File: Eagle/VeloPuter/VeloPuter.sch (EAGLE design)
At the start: 56 parts, among them IC2 B7546, IC3 B7546, Q1 4P04L04, Q10 4P04L04, Q11 BS170, Q12 4P04L04, Q13 BS170, Q14 4P04L04, Q2 BS170, Q3 BS170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

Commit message: Minor layout change
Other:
- moved on the sheet: Q3, Q4, R1
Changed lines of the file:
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@@
 <instance part="AUX_OUT" gate=".5" x="208.28" y="73.66" rot="R180"/>
 <instance part="AUX_OUT" gate=".6" x="208.28" y="66.04" rot="R180"/>
-<instance part="Q3" gate="1" x="317.5" y="162.56"/>
-<instance part="Q4" gate="G$1" x="330.2" y="167.64" rot="MR180"/>
-<instance part="R1" gate="G$1" x="322.58" y="170.18" rot="R90">
-<attribute name="OC_NEWARK" x="322.58" y="170.18" size="1.778" layer="96" display="off"/>
-<attribute name="MF" x="322.58" y="170.18" size="1.778" layer="96" display="off"/>
-<attribute name="MPN" x="322.58" y="170.18" size="1.778" layer="96" display="off"/>
+<instance part="Q3" gate="1" x="317.5" y="165.1"/>
+<instance part="Q4" gate="G$1" x="330.2" y="172.72" rot="MR180"/>
+<instance part="R1" gate="G$1" x="322.58" y="175.26" rot="R90">
+<attribute name="OC_NEWARK" x="322.58" y="175.26" size="1.778" layer="96" display="off"/>
+<attribute name="MF" x="322.58" y="175.26" size="1.778" layer="96" display="off"/>
+<attribute name="MPN" x="322.58" y="175.26" size="1.778" layer="96" display="off"/>
 </instance>
 <instance part="JP1" gate="A" x="327.66" y="149.86" rot="R270"/>
@@
 <segment>
 <pinref part="Q3" gate="1" pin="S"/>
-<wire x1="320.04" y1="157.48" x2="325.12" y2="160.02" width="0.1524" layer="91"/>
+<wire x1="320.04" y1="160.02" x2="325.12" y2="160.02" width="0.1524" layer="91"/>
 <pinref part="GND16" gate="1" pin="GND"/>
 </segment>
@@
 <pinref part="Q4" gate="G$1" pin="S"/>
 <wire x1="332.74" y1="154.94" x2="335.28" y2="154.94" width="0.1524" layer="91"/>
-<wire x1="332.74" y1="162.56" x2="332.74" y2="154.94" width="0.1524" layer="91"/>
+<wire x1="332.74" y1="167.64" x2="332.74" y2="154.94" width="0.1524" layer="91"/>
 <junction x="332.74" y="154.94"/>
 </segment>
@@
 <net name="PWM_FRONT" class="0">
 <segment>
-<wire x1="307.34" y1="165.1" x2="312.42" y2="162.56" width="0.1524" layer="91"/>
+<wire x1="307.34" y1="165.1" x2="312.42" y2="165.1" width="0.1524" layer="91"/>
 <pinref part="Q3" gate="1" pin="G"/>
 <label x="307.34" y="165.1" size="1.778" layer="95" rot="R180" xref="yes"/>
@@
 <label x="149.86" y="12.7" size="1.778" layer="95" xref="yes"/>
 <wire x1="142.24" y1="12.7" x2="149.86" y2="12.7" width="0.1524" layer="91"/>
+<junction x="142.24" y="12.7"/>
 </segment>
 </net>
@@
 <pinref part="R1" gate="G$1" pin="2"/>
 <pinref part="Q4" gate="G$1" pin="D"/>
-<wire x1="332.74" y1="175.26" x2="332.74" y2="172.72" width="0.1524" layer="91"/>
-<wire x1="332.74" y1="175.26" x2="322.58" y2="175.26" width="0.1524" layer="91"/>
+<wire x1="332.74" y1="180.34" x2="332.74" y2="177.8" width="0.1524" layer="91"/>
+<wire x1="332.74" y1="180.34" x2="322.58" y2="180.34" width="0.1524" layer="91"/>
 <label x="317.5" y="175.26" size="1.778" layer="95" rot="R180"/>
-<wire x1="317.5" y1="175.26" x2="322.58" y2="175.26" width="0.1524" layer="91"/>
-<junction x="322.58" y="175.26"/>
+<wire x1="317.5" y1="180.34" x2="322.58" y2="180.34" width="0.1524" layer="91"/>
+<junction x="322.58" y="180.34"/>
 </segment>
 <segment>
@@
 <pinref part="Q4" gate="G$1" pin="G"/>
 <pinref part="R1" gate="G$1" pin="1"/>
-<junction x="320.04" y="167.64"/>
-<wire x1="320.04" y1="167.64" x2="325.12" y2="165.1" width="0.1524" layer="91"/>
-<wire x1="322.58" y1="165.1" x2="320.04" y2="167.64" width="0.1524" layer="91"/>
-</segment>
-</net>
+<junction x="320.04" y="170.18"/>
+<wire x1="320.04" y1="170.18" x2="325.12" y2="170.18" width="0.1524" layer="91"/>
+<wire x1="322.58" y1="170.18" x2="320.04" y2="170.18" width="0.1524" layer="91"/>
+</segment>
+</net>

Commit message: Board updates
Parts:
- R6: value 1 ohm -> 1 Ω
- renumbered JP6 to JP
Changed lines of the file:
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@@
 <attribute name="OC_NEWARK" value="unknown"/>
 </part>
-<part name="R6" library="resistor" deviceset="R-EU_" device="0207/10" value="1 ohm">
+<part name="R6" library="resistor" deviceset="R-EU_" device="0207/10" value="1 Ω">
 <attribute name="MF" value=""/>
 <attribute name="MPN" value=""/>
@@
 <attribute name="OC_NEWARK" value="unknown"/>
 </part>
-<part name="JP6" library="jumper" deviceset="JP1E" device="" value=" "/>
+<part name="JP" library="jumper" deviceset="JP1E" device="" value=" "/>
 <part name="GND26" library="supply1" deviceset="GND" device=""/>
 <part name="GND27" library="supply1" deviceset="GND" device=""/>
@@
 <attribute name="MPN" x="322.58" y="-7.62" size="1.778" layer="96" display="off"/>
 </instance>
-<instance part="JP6" gate="A" x="327.66" y="-27.94" rot="R270"/>
+<instance part="JP" gate="A" x="327.66" y="-27.94" rot="R270"/>
 <instance part="GND26" gate="1" x="320.04" y="-30.48"/>
 <instance part="GND27" gate="1" x="325.12" y="-20.32"/>
@@
 <segment>
 <pinref part="GND26" gate="1" pin="GND"/>
-<pinref part="JP6" gate="A" pin="1"/>
+<pinref part="JP" gate="A" pin="1"/>
 <wire x1="320.04" y1="-27.94" x2="325.12" y2="-27.94" width="0.1524" layer="91"/>
 </segment>
@@
 <pinref part="U$1" gate="G$1" pin="DCOUT-"/>
 <pinref part="AUX_OUT" gate=".4" pin="SK"/>
-<pinref part="JP6" gate="A" pin="2"/>
+<pinref part="JP" gate="A" pin="2"/>
 <wire x1="325.12" y1="-30.48" x2="325.12" y2="-33.02" width="0.1524" layer="91"/>
 <wire x1="309.88" y1="-33.02" x2="325.12" y2="-33.02" width="0.1524" layer="91"/>

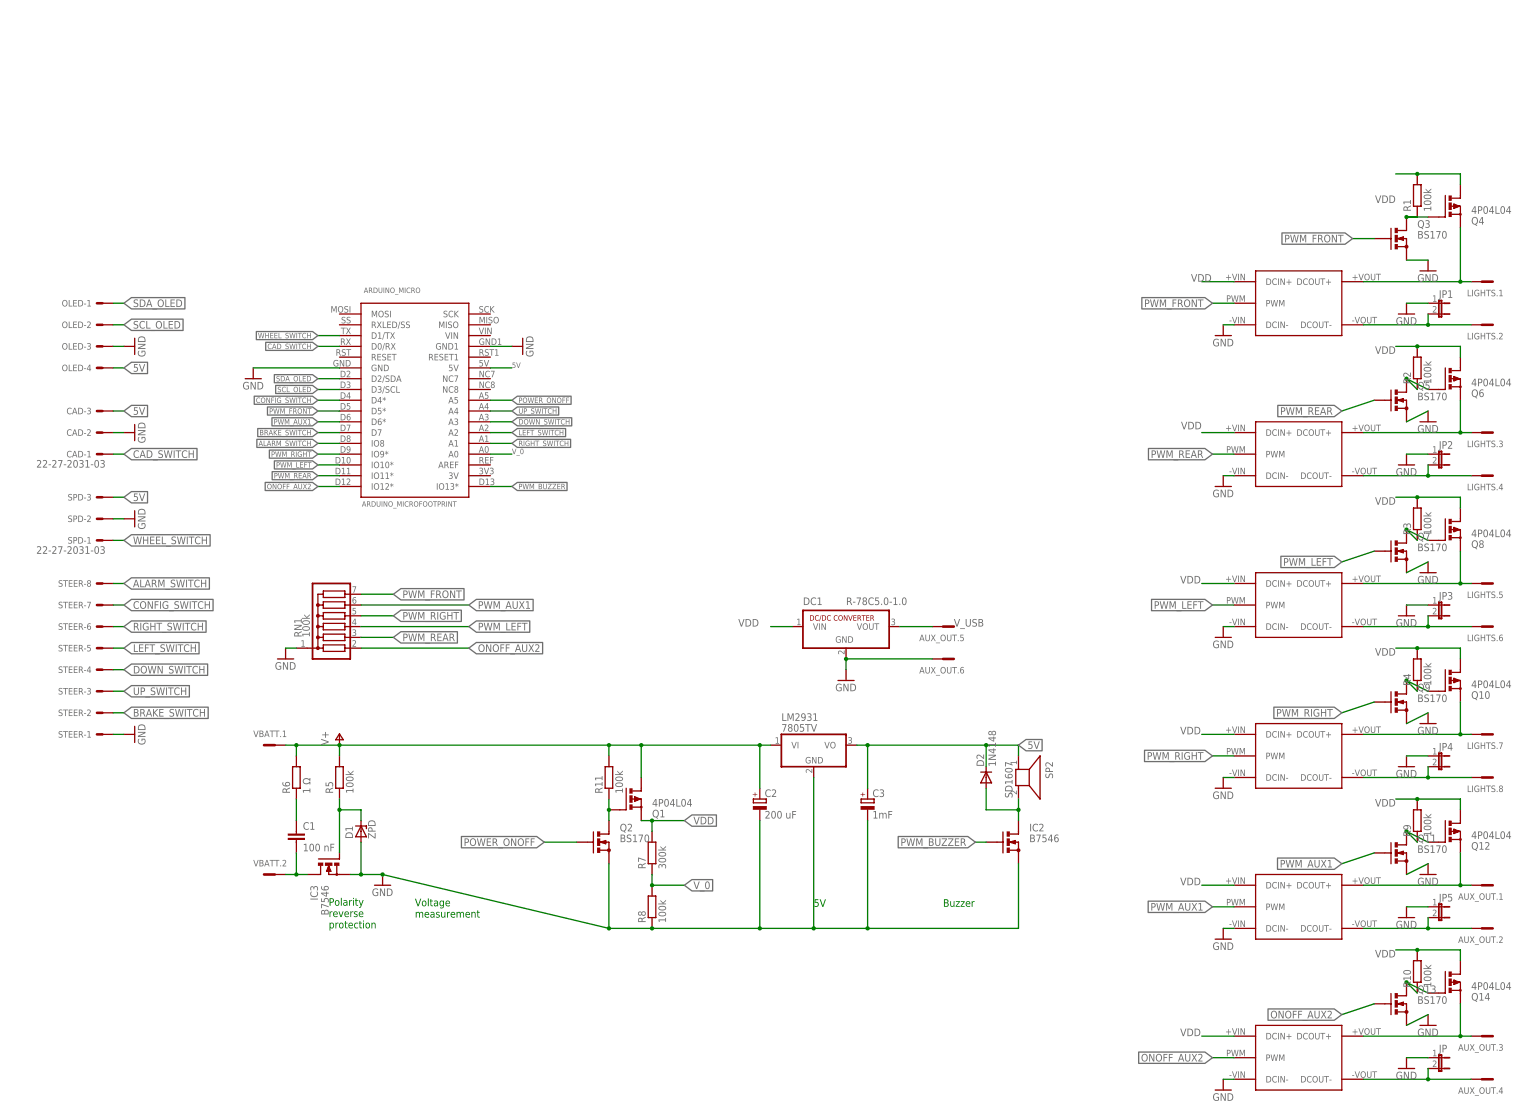
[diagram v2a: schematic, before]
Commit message: Board version 1.4 Suitable for the QV with new headlights
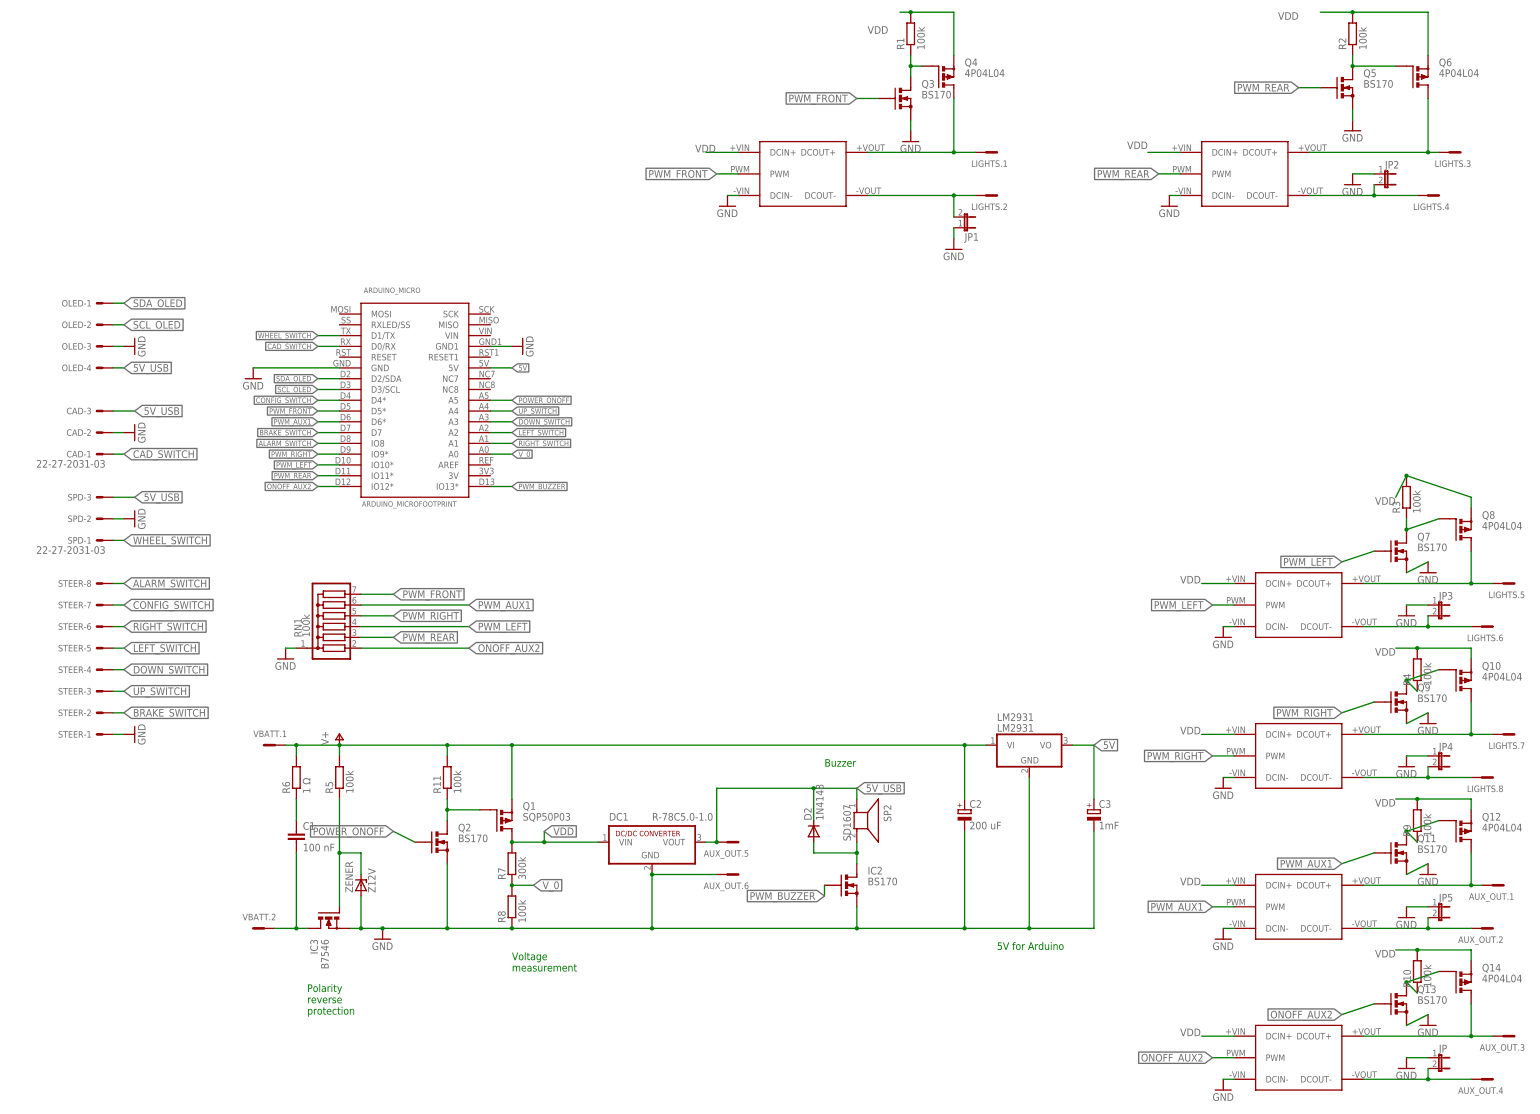
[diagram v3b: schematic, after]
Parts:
- removed D1: ZPD, diode:ZPD
- added ZENER: Z12V, diode:ZENER-DIODEDO34-7
- IC2: value B7546 -> BS170
- LM2931: value 7805TV -> LM2931
- Q1: value 4P04L04 -> SQP50P03
- R1, R10, R11, R2, R3, R4, R5, R6, R7, R8, R9: device resistor:R-EU_0207/10 -> resistor:R-EU_0207/7
- VBATT: value (none) -> VBatt
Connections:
- removed net V_USB: AUX_OUT.5.SK, DC1.VOUT
- new net 5V_USB: AUX_OUT.5.SK, CAD-3.S, D2.C, DC1.VOUT, OLED-4.S, SP2.1, SPD-3.S
- net 5V: no longer CAD-3.S, D2.C, OLED-4.S, SP2.1, SPD-3.S
- net AUX1+: now also Q12.D; no longer Q12.S
- net AUX2+: now also Q14.D; no longer Q14.S
- net FRONT+: now also Q4.D; no longer Q4.S
- net GND: now also ZENER.A; no longer D1.A
- net LEFT+: now also Q8.D; no longer Q8.S
- net N$4: now also ZENER.C; no longer D1.C
- net REAR+: now also Q6.D; no longer Q6.S
- net RIGHT+: now also Q10.D; no longer Q10.S
- net V+: now also Q1.S; no longer Q1.D
- net VDD: now also Q1.D, Q10.S, Q12.S, Q14.S, Q4.S, Q6.S, Q8.S; no longer Q1.S, Q10.D, Q12.D, Q14.D, Q4.D, Q6.D, Q8.D
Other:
- note added: "5V for Arduino"
- note removed: "5V"
- moved on the sheet: AUX_OUT.1, AUX_OUT.3, AUX_OUT.5, AUX_OUT.6, C2, C3, D2, DC1, IC2, IC3, JP1, JP2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
